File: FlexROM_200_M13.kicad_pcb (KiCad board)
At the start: 2 copper layers, 35.6 x 17.8 mm, 6 parts, among them J1 27C256 DIP LEGS, U1 28C256

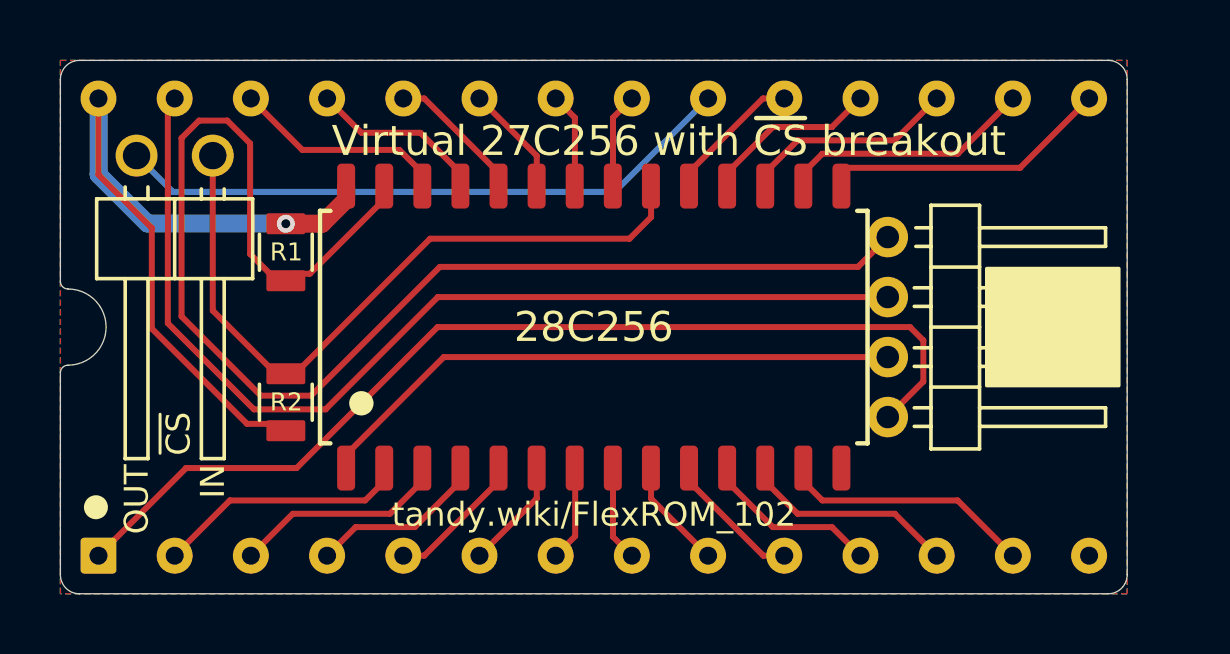
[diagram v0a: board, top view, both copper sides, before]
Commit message: add FlexROM_200_M13
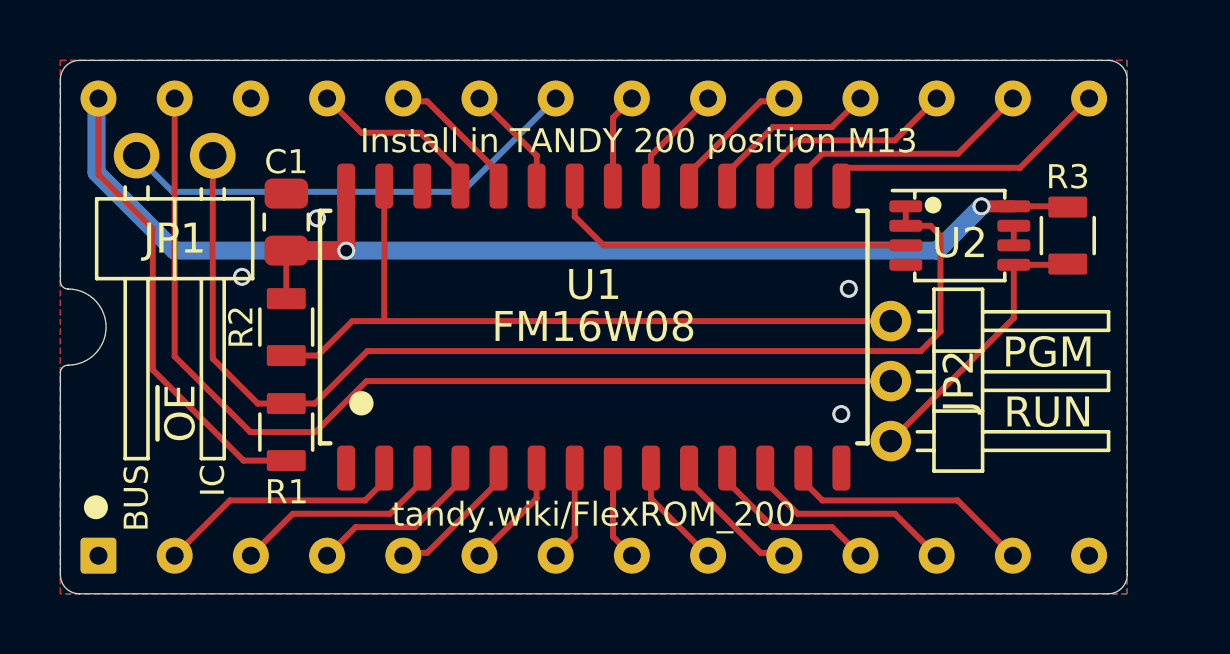
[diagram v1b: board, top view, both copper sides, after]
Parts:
- added C1: 0.1uF, 000_LOCAL:C_0805, F.Cu at (116.8, 98.1)
- added R3: 47K, 000_LOCAL:R_0805, F.Cu at (142.8, 98.5)
- added U2: 74LVC2G00, 000_LOCAL:SSOP-8_2.95x2.8x0.65, F.Cu at (139.2, 98.5)
- J1: value 27C256 DIP LEGS -> HN61364_TANDY_200_M13
- JP1: value ~{CS} breakout (REX TP1) -> Jumper_2_bridged
- JP2: value Jumper_4_Bridged23 -> Jumper_3_Bridged23; footprint 000_LOCAL:PinHeader_1x04_P2.00mm_Horizontal -> 000_LOCAL:PinHeader_1x03_P2.00mm_Horizontal
- U1: value 28C256 -> FM16W08
- moved JP2 2.80 mm to (136.9, 101.4)
- moved R2 2.50 mm to (116.8, 101.6)
- moved R1 1.00 mm to (116.8, 105.1)
- renumbered R2 to R1, R1 to R2
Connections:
- net /A14_~{WE} renamed /OE1/~{WE}
- J1 pad 1: /NC_A14 -> unconnected-(J1-Pad1)
- J1 pad 20: /~{CS_OUT} -> /~{CS}
- J1 pad 22: /~{OE} -> /~{OE0}_bus
- J1 pad 26: /A13 -> unconnected-(J1-Pad26)
- JP1 pad 1: /~{CS_IN} -> /~{OE0}
- JP1 pad 2: /~{CS_OUT} -> /~{OE0}_bus
- JP2 pad 3: /A14 -> /OE1
- R1 pad 1: /~{CS_IN} -> /~{OE0}
- U1 pad 1: /A14 -> GND
- U1 pad 20: /~{CS_IN} -> /~{CS}
- U1 pad 26: /A13 -> GND
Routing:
- net /~{OE0}: track 0.00 -> 37.8 mm
- net /NC_A14: track 33.9 -> 0.00 mm
- net VCC: track 26.5 -> 57.8 mm, vias 1 -> 2
- net /~{CS_IN}: track 23.8 -> 0.00 mm
- net /~{CS_OUT}: track 20.8 -> 0.00 mm
- net /~{WE}: track 45.7 -> 25.2 mm
- net /A14: track 19.8 -> 0.00 mm
- net /~{OE0}_bus: track 0.00 -> 15.8 mm
- net /OE1: track 0.00 -> 9.38 mm
- net /~{OE}: track 3.18 -> 12.4 mm
- net /A13: track 7.19 -> 0.00 mm
- net /~{CS}: track 0.00 -> 3.71 mm
- net Net-(U2-Pad6): track 0.00 -> 0.65 mm
- net GND: vias 0 -> 4
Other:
- board text added: "BUS"
- board text added: "Boot from internal main rom: Connect ~{OE}_BUS to ~{OE}_IC Boot from REX_Classic main rom: Connect ~{OE}_BUS to REX TP2"
- board text added: "IC"
- board text added: "Install in TANDY 200 position M13"
- board text added: "PGM"
- board text added: "PROG-("
- board text added: "R1,R2,R3: ${00000000-0000-0000-0000-00005f9fca43:VALUE} C1: ${9745923e-b3f3-4f78-9da8-cbeee6cd8cf3:VALUE} U2: ${7d0efb14-35d7-40aa-96f5-408b9024bd0a:VALUE} Legs: TE 1544210"
- board text added: "RUN-("
- board text added: "tandy.wiki/FlexROM_200"
- board text added: "~{OE}"
- board text removed: "Boot from internal main rom: Connect ~{CS}_OUT to ~{CS}_IN Boot from REX_Classic main rom: Connect ~{CS}_OUT to REX TP1"
- board text removed: "IN"
- board text removed: "OUT"
- board text removed: "PROGRAM"
- board text removed: "R1,R2: ${00000000-0000-0000-0000-00005f9fca43:VALUE} Legs: TE 1544210"
- board text removed: "Virtual 27C256 with ~{CS} breakout"
- board text removed: "tandy.wiki/FlexROM_102"
- board text removed: "~{CS}"

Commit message: flexrom 102 & 200 accept eeprom or fram
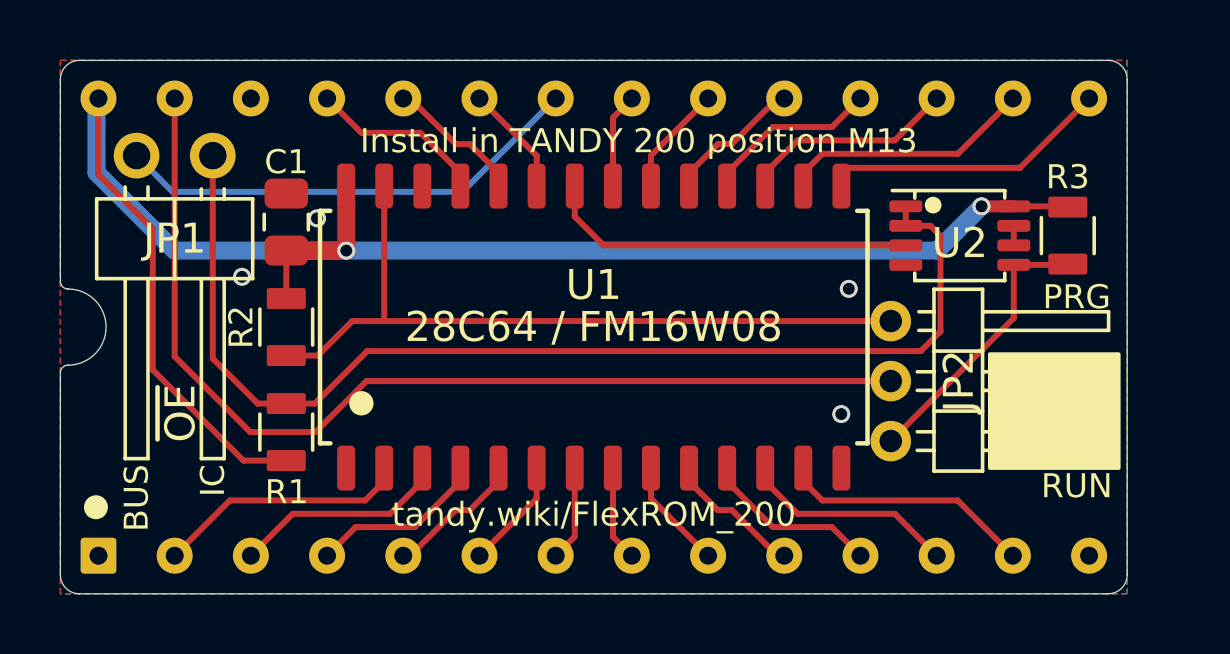
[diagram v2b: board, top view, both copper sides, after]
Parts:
- U1: value FM16W08 -> 28C64 / FM16W08
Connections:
- net Net-(U2-Pad6) renamed /OE0
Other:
- board text added: "PRG"
- board text added: "R1,R2,R3: ${00000000-0000-0000-0000-00005f9fca43:VALUE} C1: ${9745923e-b3f3-4f78-9da8-cbeee6cd8cf3:VALUE} U2: ${7d0efb14-35d7-40aa-96f5-408b9024bd0a:VALUE} Legs: TE 1544210 or Mill-Max 3121"
- board text added: "To boot from EEPROM/FRAM: Connect ~{OE}_BUS to ~{OE}_IC To boot from REX_Classic: Connect ~{OE}_BUS to REX TP2"
- board text removed: "Boot from internal main rom: Connect ~{OE}_BUS to ~{OE}_IC Boot from REX_Classic main rom: Connect ~{OE}_BUS to REX TP2"
- board text removed: "PGM"
- board text removed: "R1,R2,R3: ${00000000-0000-0000-0000-00005f9fca43:VALUE} C1: ${9745923e-b3f3-4f78-9da8-cbeee6cd8cf3:VALUE} U2: ${7d0efb14-35d7-40aa-96f5-408b9024bd0a:VALUE} Legs: TE 1544210"
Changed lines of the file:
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@@
   (title_block
     (title "FlexROM_200_M13")
-    (date "2022-11-15")
-    (rev "001")
+    (date "2022-11-30")
+    (rev "002")
     (company "Brian K. White - b.kenyon.w@gmail.com")
+    (comment 1 "CC-BY-SA")
     (comment 2 "github.com/bkw777/aDIPters")
   )
@@
   (net 28 "/OE1")
   (net 29 "/~{CS}")
-  (net 30 "Net-(U2-Pad6)")
+  (net 30 "/OE0")
   (net 31 "unconnected-(J1-Pad1)")
   (net 32 "unconnected-(J1-Pad26)")
@@
       (effects (font (size 1 1) (thickness 0.15)))
     )
-    (fp_text value "FM16W08" (at -0.0003 -0.0002) (layer "F.SilkS")
+    (fp_text value "28C64 / FM16W08" (at -0.0003 -0.0002) (layer "F.SilkS")
       (effects (font (size 1 1) (thickness 0.15)))
     )
@@
       (net 28 "/OE1") (pintype "input"))
     (pad "6" smd roundrect (at 1.8 0.325 270) (size 0.4 1.1) (layers "F.Cu" "F.Paste" "F.Mask") (roundrect_rratio 0.25)
-      (net 30 "Net-(U2-Pad6)") (pintype "input"))
+      (net 30 "/OE0") (pintype "input"))
     (pad "7" smd roundrect (at 1.8 -0.325 270) (size 0.4 1.1) (layers "F.Cu" "F.Paste" "F.Mask") (roundrect_rratio 0.25)
-      (net 30 "Net-(U2-Pad6)") (pintype "output"))
+      (net 30 "/OE0") (pintype "output"))
     (pad "8" smd roundrect (at 1.8 -0.975 270) (size 0.4 1.1) (layers "F.Cu" "F.Paste" "F.Mask") (roundrect_rratio 0.25)
       (net 26 "VCC") (pinfunction "VCC") (pintype "power_in"))
@@
   )
   (gr_circle (center 110.405 107.605) (end 110.405 107.405) (layer "F.SilkS") (width 0.4) (fill none))
-  (gr_text "R1,R2,R3: ${00000000-0000-0000-0000-00005f9fca43:VALUE}    C1: ${9745923e-b3f3-4f78-9da8-cbeee6cd8cf3:VALUE}\nU2: ${7d0efb14-35d7-40aa-96f5-408b9024bd0a:VALUE}   Legs: TE 1544210" (at 144.145 107.315) (layer "B.SilkS")
+  (gr_rect (start 140.2 102.5) (end 144.5 106.3) (layer "F.SilkS") (width 0.12) (fill solid))
+  (gr_text "R1,R2,R3: ${00000000-0000-0000-0000-00005f9fca43:VALUE}    C1: ${9745923e-b3f3-4f78-9da8-cbeee6cd8cf3:VALUE}\nU2: ${7d0efb14-35d7-40aa-96f5-408b9024bd0a:VALUE}   Legs: TE 1544210 or Mill-Max 3121" (at 144.145 107.315) (layer "B.SilkS")
     (effects (font (size 0.6 0.6) (thickness 0.08)) (justify left mirror))
   )
@@
     (effects (font (size 1 1) (thickness 0.15)) (justify right mirror))
   )
-  (gr_text "Boot from internal main rom:\n  Connect ~{OE}_BUS to ~{OE}_IC\n\nBoot from REX_Classic main rom:\n  Connect ~{OE}_BUS to REX TP2" (at 133.65 102.2) (layer "B.SilkS")
+  (gr_text "To boot from EEPROM/FRAM:\n  Connect ~{OE}_BUS to ~{OE}_IC\n\nTo boot from REX_Classic:\n  Connect ~{OE}_BUS to REX TP2" (at 133.65 102.2) (layer "B.SilkS")
     (effects (font (size 0.8 0.8) (thickness 0.1)) (justify left mirror))
   )
@@
     (effects (font (size 0.8 0.8) (thickness 0.12)))
   )
+  (gr_text "PRG" (at 143.1 100.6) (layer "F.SilkS")
+    (effects (font (size 0.8 0.8) (thickness 0.1)))
+  )
   (gr_text "BUS" (at 111.76 106.172 90) (layer "F.SilkS")
     (effects (font (size 0.8 0.8) (thickness 0.1)) (justify right))
   )
-  (gr_text "PGM" (at 142.15 102.45) (layer "F.SilkS")
-    (effects (font (size 1 1) (thickness 0.15)))
-  )
   (gr_text "IC" (at 114.3 106.172 90) (layer "F.SilkS")
     (effects (font (size 0.8 0.8) (thickness 0.1)) (justify right))
   )
-  (gr_text "RUN" (at 142.15 104.45) (layer "F.SilkS")
-    (effects (font (size 1 1) (thickness 0.15)))
+  (gr_text "RUN" (at 143.1 106.9) (layer "F.SilkS")
+    (effects (font (size 0.8 0.8) (thickness 0.1)))
   )
   (segment (start 143.515 93.985) (end 141.2086 96.2914) (width 0.2) (layer "F.Cu") (net 1))
@@
   (segment (start 131.45 96.4515) (end 131.45 96.905) (width 0.2) (layer "F.Cu") (net 7))
   (segment (start 134.9375 94.9325) (end 132.969 94.9325) (width 0.2) (layer "F.Cu") (net 7))
-  (segment (start 120.65 109.22) (end 120.745 109.125) (width 0.2) (layer "F.Cu") (net 8))
-  (segment (start 121.4435 109.125) (end 123.83 106.7385) (width 0.2) (layer "F.Cu") (net 8))
+  (segment (start 120.88 109.22) (end 122.4 107.7) (width 0.2) (layer "F.Cu") (net 8))
+  (segment (start 122.8685 107.7) (end 123.83 106.7385) (width 0.2) (layer "F.Cu") (net 8))
+  (segment (start 122.4 107.7) (end 122.8685 107.7) (width 0.2) (layer "F.Cu") (net 8))
   (segment (start 123.83 106.7385) (end 123.83 106.305) (width 0.2) (layer "F.Cu") (net 8))
-  (segment (start 120.745 109.125) (end 121.4435 109.125) (width 0.2) (layer "F.Cu") (net 8))
-  (segment (start 132.5692 94.075) (end 133.255 94.075) (width 0.2) (layer "F.Cu") (net 9))
-  (segment (start 130.175 96.4692) (end 132.5692 94.075) (width 0.2) (layer "F.Cu") (net 9))
+  (segment (start 120.65 109.22) (end 120.88 109.22) (width 0.2) (layer "F.Cu") (net 8))
   (segment (start 130.175 96.9) (end 130.175 96.4692) (width 0.2) (layer "F.Cu") (net 9))
-  (segment (start 133.255 94.075) (end 133.35 93.98) (width 0.2) (layer "F.Cu") (net 9))
+  (segment (start 133.12 93.98) (end 133.35 93.98) (width 0.2) (layer "F.Cu") (net 9))
+  (segment (start 130.175 96.4692) (end 131.1442 95.5) (width 0.2) (layer "F.Cu") (net 9))
+  (segment (start 131.6 95.5) (end 133.12 93.98) (width 0.2) (layer "F.Cu") (net 9))
+  (segment (start 131.1442 95.5) (end 131.6 95.5) (width 0.2) (layer "F.Cu") (net 9))
   (segment (start 125.095 107.315) (end 125.095 106.3) (width 0.2) (layer "F.Cu") (net 10))
   (segment (start 123.19 109.22) (end 125.095 107.315) (width 0.2) (layer "F.Cu") (net 10))
@@
   (segment (start 125.1 96.905) (end 125.1 95.89) (width 0.2) (layer "F.Cu") (net 16))
   (segment (start 125.1 95.89) (end 123.195 93.985) (width 0.2) (layer "F.Cu") (net 16))
-  (segment (start 133.255 109.125) (end 133.35 109.22) (width 0.2) (layer "F.Cu") (net 17))
+  (segment (start 131.6 107.7) (end 133.12 109.22) (width 0.2) (layer "F.Cu") (net 17))
+  (segment (start 131.1315 107.7) (end 131.6 107.7) (width 0.2) (layer "F.Cu") (net 17))
   (segment (start 130.18 106.305) (end 130.18 106.7485) (width 0.2) (layer "F.Cu") (net 17))
-  (segment (start 130.18 106.7485) (end 132.5565 109.125) (width 0.2) (layer "F.Cu") (net 17))
-  (segment (start 132.5565 109.125) (end 133.255 109.125) (width 0.2) (layer "F.Cu") (net 17))
+  (segment (start 130.18 106.7485) (end 131.1315 107.7) (width 0.2) (layer "F.Cu") (net 17))
+  (segment (start 133.12 109.22) (end 133.35 109.22) (width 0.2) (layer "F.Cu") (net 17))
   (segment (start 123.825 96.4565) (end 123.825 96.9) (width 0.2) (layer "F.Cu") (net 18))
-  (segment (start 120.655 93.985) (end 120.745 94.075) (width 0.2) (layer "F.Cu") (net 18))
-  (segment (start 120.745 94.075) (end 121.4435 94.075) (width 0.2) (layer "F.Cu") (net 18))
-  (segment (start 121.4435 94.075) (end 123.825 96.4565) (width 0.2) (layer "F.Cu") (net 18))
+  (segment (start 120.885 93.985) (end 122.4 95.5) (width 0.2) (layer "F.Cu") (net 18))
+  (segment (start 122.4 95.5) (end 122.8685 95.5) (width 0.2) (layer "F.Cu") (net 18))
+  (segment (start 122.8685 95.5) (end 123.825 96.4565) (width 0.2) (layer "F.Cu") (net 18))
+  (segment (start 120.655 93.985) (end 120.885 93.985) (width 0.2) (layer "F.Cu") (net 18))
   (segment (start 134.9375 108.2675) (end 135.895 109.225) (width 0.2) (layer "F.Cu") (net 19))
   (segment (start 131.445 106.3) (end 131.445 106.745) (width 0.2) (layer "F.Cu") (net 19))
@@
   (segment (start 131.445 106.745) (end 132.9675 108.2675) (width 0.2) (layer "F.Cu") (net 19))
   (segment (start 122.56 96.905) (end 122.56 96.4615) (width 0.2) (layer "F.Cu") (net 20))
-  (segment (start 119.253 95.123) (end 118.115 93.985) (width 0.2) (layer "F.Cu") (net 20))
+  (segment (start 119.253 95.123) (end 118.11 93.98) (width 0.2) (layer "F.Cu") (net 20))
   (segment (start 121.2215 95.123) (end 119.253 95.123) (width 0.2) (layer "F.Cu") (net 20))
   (segment (start 122.56 96.4615) (end 121.2215 95.123) (width 0.2) (layer "F.Cu") (net 20))
@@
   (segment (start 122.6185 97.0915) (end 125.73 93.98) (width 0.2) (layer "B.Cu") (net 27))
   (segment (start 112.9665 97.0915) (end 122.6185 97.0915) (width 0.2) (layer "B.Cu") (net 27))
+  (segment (start 136.9 105.4) (end 141 101.3) (width 0.2) (layer "F.Cu") (net 28))
+  (segment (start 142.775 99.525) (end 142.8 99.5) (width 0.2) (layer "F.Cu") (net 28))
   (segment (start 141 101.3) (end 141 99.525) (width 0.2) (layer "F.Cu") (net 28))
-  (segment (start 142.775 99.525) (end 142.8 99.5) (width 0.2) (layer "F.Cu") (net 28))
   (segment (start 141 99.525) (end 142.775 99.525) (width 0.2) (layer "F.Cu") (net 28))
-  (segment (start 136.9 105.4) (end 141 101.3) (width 0.2) (layer "F.Cu") (net 28))
   (segment (start 128.905 95.885) (end 130.81 93.98) (width 0.2) (layer "F.Cu") (net 29))
   (segment (start 128.905 96.9) (end 128.905 95.885) (width 0.2) (layer "F.Cu") (net 29))
